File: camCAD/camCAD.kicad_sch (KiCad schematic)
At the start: 0 parts

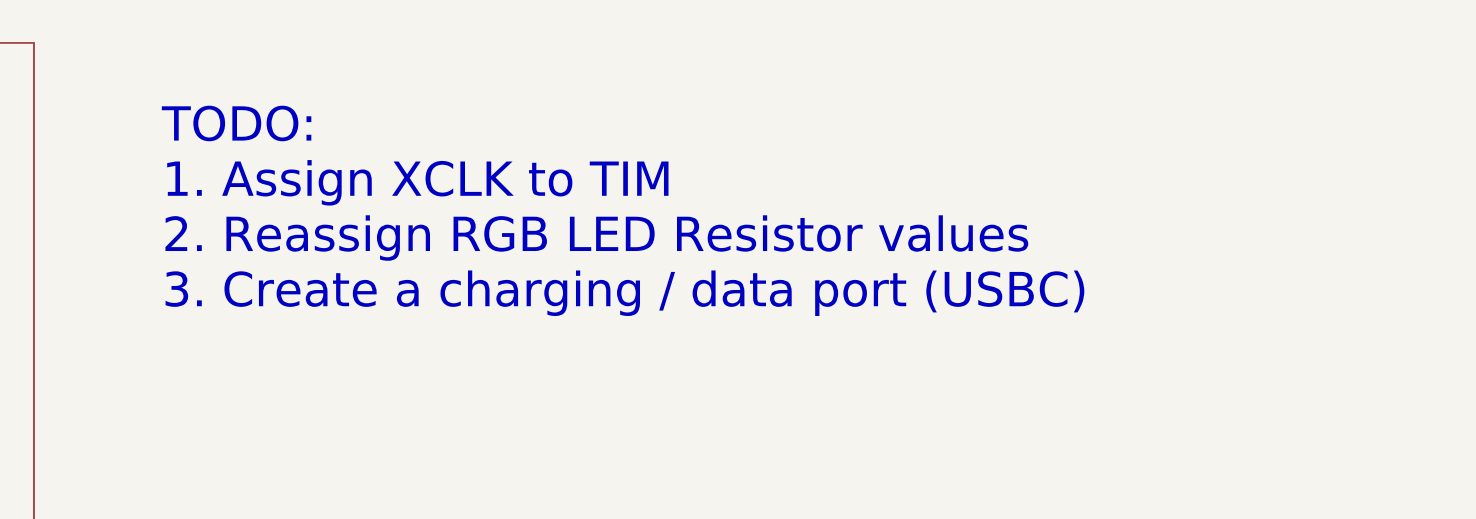
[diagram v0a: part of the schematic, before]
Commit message: Added footprints for major components, renamed some components for more specific information
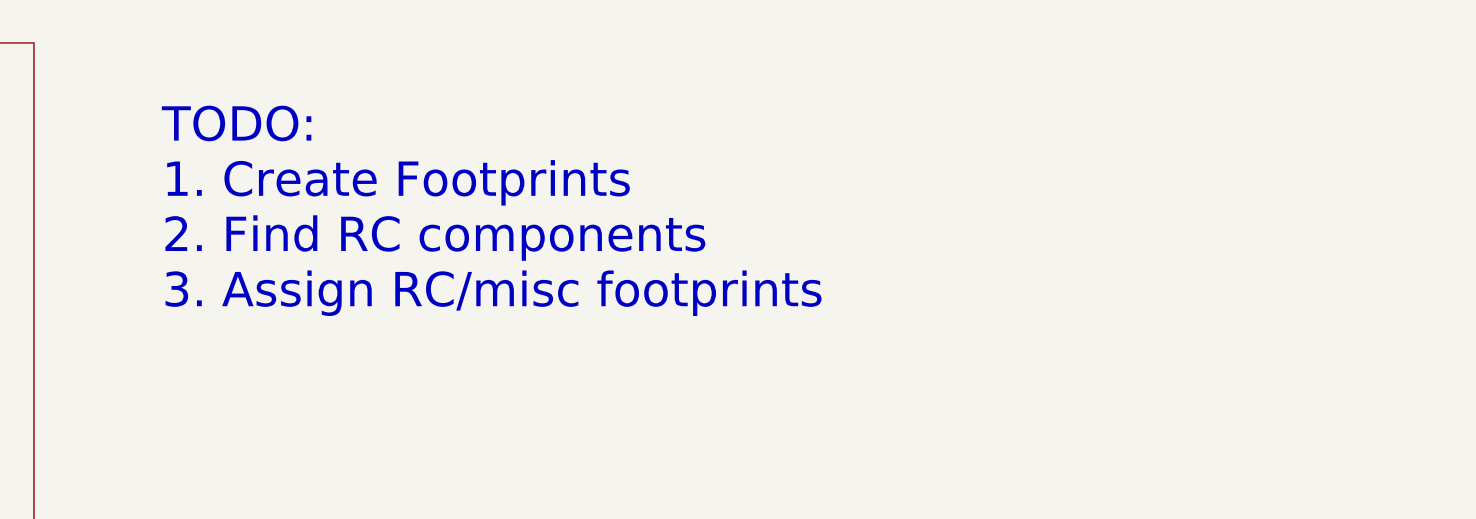
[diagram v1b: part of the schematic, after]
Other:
- note added: "TODO: 1. Create Footprints 2. Find RC components 3. Assign RC/misc footprints"
- note removed: "TODO: 1. Assign XCLK to TIM 2. Reassign RGB LED Resistor values 3. Create a charging / data port (USBC)"
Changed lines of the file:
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@@
 		(comment 4 "By Siddharth Vasudevan")
 	)
-	(text "TODO:\n1. Assign XCLK to TIM\n2. Reassign RGB LED Resistor values\n3. Create a charging / data port (USBC)\n"
+	(text "TODO:\n1. Create Footprints\n2. Find RC components\n3. Assign RC/misc footprints\n"
 		(exclude_from_sim no)
 		(at 245.364 47.752 0)

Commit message: Started PCB Layout, need to add a user interface
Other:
- added sheet UI (user_interface.kicad_sch)
- note added: "TODO: 1. User interface??"
- note removed: "TODO: 1. Create Footprints 2. Find RC components 3. Assign RC/misc footprints"
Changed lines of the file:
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@@
 		(comment 4 "By Siddharth Vasudevan")
 	)
-	(text "TODO:\n1. Create Footprints\n2. Find RC components\n3. Assign RC/misc footprints\n"
+	(text "TODO:\n1. User interface??"
 		(exclude_from_sim no)
-		(at 245.364 47.752 0)
+		(at 244.094 157.734 0)
 		(effects
 			(font
@@
 			)
 			(justify left)
+		)
+	)
+	(sheet
+		(at 243.84 29.21)
+		(size 112.395 100.33)
+		(exclude_from_sim no)
+		(in_bom yes)
+		(on_board yes)
+		(dnp no)
+		(fields_autoplaced yes)
+		(stroke
+			(width 0.1524)
+			(type solid)
+		)
+		(fill
+			(color 0 0 0 0)
+		)
+		(property "Sheetname" "UI"
+			(at 243.84 28.4984 0)
+			(show_name no)
+			(do_not_autoplace no)
+			(effects
+				(font
+					(size 1.27 1.27)
+				)
+				(justify left bottom)
+			)
+		)
+		(property "Sheetfile" "user_interface.kicad_sch"
+			(at 243.84 130.1246 0)
+			(show_name no)
+			(do_not_autoplace no)
+			(effects
+				(font
+					(size 1.27 1.27)
+				)
+				(justify left top)
+			)
+		)
+		(instances
+			(project "camCAD"
+				(path "/e2824ea6-9024-4cee-b80c-5fefbc7112d7"
+					(page "6")
+				)
+			)
 		)
 	)
@@
 	)
 	(sheet
-		(at 129.54 29.21)
+		(at 127 29.21)
 		(size 101.6 100.965)
 		(exclude_from_sim no)
@@
 		)
 		(property "Sheetname" "Components"
-			(at 129.54 28.4984 0)
+			(at 127 28.4984 0)
 			(show_name no)
 			(do_not_autoplace no)
@@
 		)
 		(property "Sheetfile" "components.kicad_sch"
-			(at 129.54 130.7596 0)
+			(at 127 130.7596 0)
 			(show_name no)
 			(do_not_autoplace no)
@@
 	)
 	(sheet
-		(at 129.54 149.86)
+		(at 127 149.86)
 		(size 102.235 96.52)
 		(exclude_from_sim no)
@@
 		)
 		(property "Sheetname" "Power_Supply&Charging"
-			(at 129.54 149.1484 0)
+			(at 127 149.1484 0)
 			(show_name no)
 			(do_not_autoplace no)
@@
 		)
 		(property "Sheetfile" "buck.kicad_sch"
-			(at 129.54 246.9646 0)
+			(at 127 246.9646 0)
 			(show_name no)
 			(do_not_autoplace no)
